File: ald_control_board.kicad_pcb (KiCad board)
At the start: 2 copper layers, 70 parts, among them J1 PWR_24V_IN, J10 MFC_DB15, J11 VACUUM_GAUGE_8PIN, J2 PWR_12V_IN, J3 PWR_5V_IN, J4 PWR_±15V_IN, J5 J_FORELINE_VALVE, J6 J_PRECURSOR_A, J7 J_N2_PURGE, J8 J_SPARE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

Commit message: im so happy
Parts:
- removed TP2: TestPoint, TestPoint:TestPoint_Loop_D2.50mm_Drill1.0mm
- moved TP3 101.0 mm to (228.4, 125.0)
- moved TP7 97.0 mm to (224.7, 137.0)
- moved C12 94.8 mm to (212.2, 135.4), turned to 180 degrees
- moved R3 94.6 mm to (216.5, 125.2)
- moved R6 93.6 mm to (216.5, 135.4)
- moved TP5 89.6 mm to (216.8, 130.2)
- moved J9 87.5 mm to (220.7, 122.6)
- moved R7 82.0 mm to (225.3, 141.1), turned to 180 degrees
- moved R2 81.9 mm to (224.7, 122.4)
- moved C13 81.3 mm to (230.0, 141.1)
- moved TP1 78.2 mm to (216.5, 122.2)
- moved TP8 76.7 mm to (215.4, 139.7)
- moved R4 76.5 mm to (224.7, 127.8), turned to 180 degrees
- moved R5 75.3 mm to (224.7, 132.9), turned to 180 degrees
- moved C11 75.2 mm to (229.6, 132.9)
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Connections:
- C1 pad 1: GND_PWR -> +24V
- C10 pad 2: /power_input/-15V -> -15V
- C12 pad 1: /daq_interface/AI_PRESSURE_FILT -> /vacuum_gauge_interface/AI_PRESSURE_FILT
- C2 pad 2: GND_PWR -> +24V
- C20 pad 1: /vacuum_gauge_interface/+24V -> +24V
- C21 pad 1: /vacuum_gauge_interface/+24V -> +24V
- C3 pad 2: GND_PWR -> +12V
- C4 pad 1: GND_PWR -> +12V
- C5 pad 1: GND_SIG -> +5V
- C6 pad 1: GND_SIG -> +5V
- C7 pad 1: /power_input/+15V -> +15V
- C8 pad 1: /power_input/+15V -> +15V
- C9 pad 1: /power_input/-15V -> -15V
- F1 pad 2: /power_input/+24V_IN -> +24V
- F2 pad 2: /power_input/+12V_IN -> +12V
- J1 pad 1: /power_input/+24V_IN -> +24V
- J11 pad 1: /vacuum_gauge_interface/+24V -> +24V
- J2 pad 1: /power_input/+12V_IN -> +12V
- J3 pad 1: GND_SIG -> +5V
- J4 pad 1: /power_input/+15V -> +15V
- J4 pad 3: /power_input/-15V -> -15V
- J5 pad 2: GNDPWR -> GND_PWR
- J9 pad 6: /daq_interface/AI_PRESSURE -> /vacuum_gauge_interface/AI_PRESSURE
- K1 pad 1: (no net) -> Net-(J6-Pin_1)
- K1 pad 2: (no net) -> /relay_board/P0.1
- K1 pad 3: (no net) -> GND_PWR
- K1 pad 5: (no net) -> +24V
- K2 pad 1: (no net) -> Net-(J5-Pin_1)
- K2 pad 2: (no net) -> /relay_board/P0.0
- K2 pad 3: (no net) -> GND_PWR
- K2 pad 5: (no net) -> +12V
- K3 pad 1: (no net) -> Net-(J7-Pin_1)
- K3 pad 3: (no net) -> GND_PWR
- K3 pad 5: (no net) -> +24V
- K4 pad 1: (no net) -> Net-(J8-Pin_1)
- K4 pad 2: (no net) -> /relay_board/P0.3
- K4 pad 3: (no net) -> GND_PWR
- K4 pad 5: (no net) -> +24V
- R6 pad 1: /daq_interface/AI_PRESSURE_FILT -> /vacuum_gauge_interface/AI_PRESSURE_FILT
- R6 pad 2: /daq_interface/AI_PRESSURE -> /vacuum_gauge_interface/AI_PRESSURE
- R8 pad 1: AO_MFC_SETPOINT -> /daq_interface/AO_MFC_SETPOINT
- R9 pad 1: AI_MFC_FLOW -> /daq_interface/AI_MFC_FLOW
- TP15 pad 1: /vacuum_gauge_interface/+24V -> +24V
- TP7 pad 1: /daq_interface/AI_PRESSURE -> /vacuum_gauge_interface/AI_PRESSURE
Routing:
- net +24V: track 0.00 -> 302.2 mm
- net +15V: track 0.00 -> 287.1 mm
- net -15V: track 0.00 -> 267.0 mm
- net +12V: track 0.00 -> 113.0 mm
- net /daq_interface/AI_MFC_FLOW: track 0.00 -> 102.9 mm
- net /daq_interface/AO_MFC_SETPOINT: track 0.00 -> 90.1 mm
- net GND_PWR: track 0.00 -> 88.3 mm, vias 0 -> 2
- net Net-(J8-Pin_1): track 0.00 -> 28.0 mm
- net Net-(J6-Pin_1): track 0.00 -> 27.5 mm
- net Net-(J7-Pin_1): track 0.00 -> 27.3 mm
- net Net-(J5-Pin_1): track 0.00 -> 26.7 mm
- net GND_SIG: track 0.00 -> 19.1 mm
- net +5V: track 0.00 -> 16.4 mm
- net Net-(C15-Pad1): track 0.00 -> 16.3 mm
- net CHASSIS_GND: track 0.00 -> 15.5 mm, vias 0 -> 1
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- added copper zone on B.Cu, net CHASSIS_GND
- added copper zone on B.Cu, net GND_PWR
- added copper zone on B.Cu, net GND_SIG
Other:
- board outline added: 204.9 x 111.1 mm

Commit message: Hopefully finalized PCB design and other files
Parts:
- added REF**: MountingHole_3.2mm_M3_Pad_Via, MountingHole:MountingHole_3.2mm_M3_Pad_Via, F.Cu at (61.5, 47.5)
- added REF**: MountingHole_3.2mm_M3_Pad_Via, MountingHole:MountingHole_3.2mm_M3_Pad_Via, F.Cu at (252.0, 47.0)
- added REF**: MountingHole_3.2mm_M3_Pad_Via, MountingHole:MountingHole_3.2mm_M3_Pad_Via, F.Cu at (62.0, 145.0)
- added REF**: MountingHole_3.2mm_M3_Pad_Via, MountingHole:MountingHole_3.2mm_M3_Pad_Via, F.Cu at (252.5, 145.0)
- moved TP13 33.7 mm to (221.0, 78.0)
- moved C7 15.9 mm to (76.5, 117.0)
- moved C9 15.9 mm to (84.0, 117.5)
- moved C10 15.9 mm to (84.9, 124.5)
- moved C8 15.9 mm to (75.5, 125.5)
- moved J3 7.27 mm to (66.0, 100.0), turned to -90 degrees
- moved J2 5.50 mm to (66.0, 86.5), turned to -90 degrees
- moved C5 5.28 mm to (82.4, 103.0)
- moved C6 5.28 mm to (75.0, 103.0)
- moved J1 5.17 mm to (65.3, 63.0), turned to -90 degrees
- moved J5 4.81 mm to (161.5, 61.5), turned to 180 degrees
- moved J7 4.54 mm to (160.0, 106.1), turned to 90 degrees
- moved J4 4.15 mm to (66.5, 116.4), turned to -90 degrees
- moved C2 3.65 mm to (66.0, 56.0)
- moved J6 2.79 mm to (159.5, 84.1), turned to 90 degrees
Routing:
- net GND_SIG: track 19.1 -> 410.5 mm, vias 0 -> 11
- net GND_PWR: track 88.3 -> 279.4 mm, vias 2 -> 4
- net /vacuum_gauge_interface/AI_PRESSURE_FILT: track 5.55 -> 118.2 mm, vias 0 -> 2
- net /vacuum_gauge_interface/AI_PRESSURE: track 13.7 -> 106.0 mm, vias 0 -> 2
- net +15V: track 287.1 -> 238.6 mm, vias 0 -> 2
- net -15V: track 267.0 -> 222.4 mm, vias 0 -> 4
- net +24V: track 302.2 -> 293.0 mm
- net +12V: track 113.0 -> 106.7 mm
- net Net-(J5-Pin_1): track 26.7 -> 32.9 mm
- net Net-(J6-Pin_1): track 27.5 -> 33.1 mm
- net Net-(C18-Pad1): track 0.00 -> 5.44 mm
- net Net-(C16-Pad2): track 0.00 -> 4.68 mm
- net Net-(C14-Pad1): track 13.5 -> 16.9 mm
- net Net-(C15-Pad1): track 16.3 -> 18.7 mm
- net +5V: track 16.4 -> 18.1 mm
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
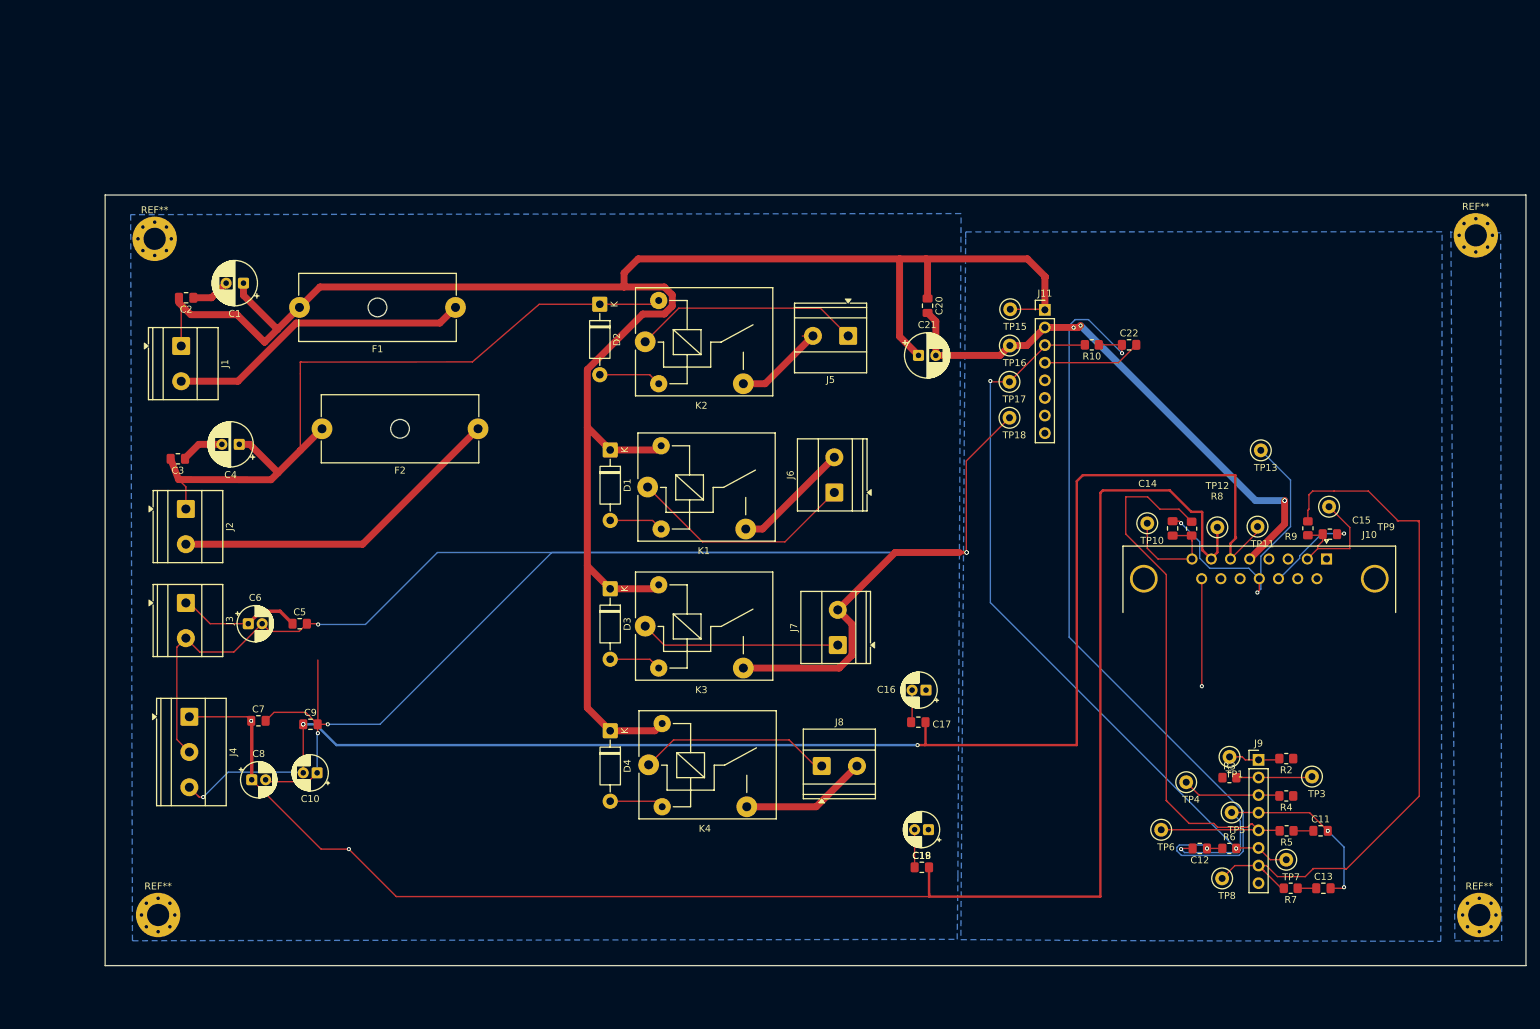
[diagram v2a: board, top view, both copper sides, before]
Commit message: rotated MFC and 10 pin daq
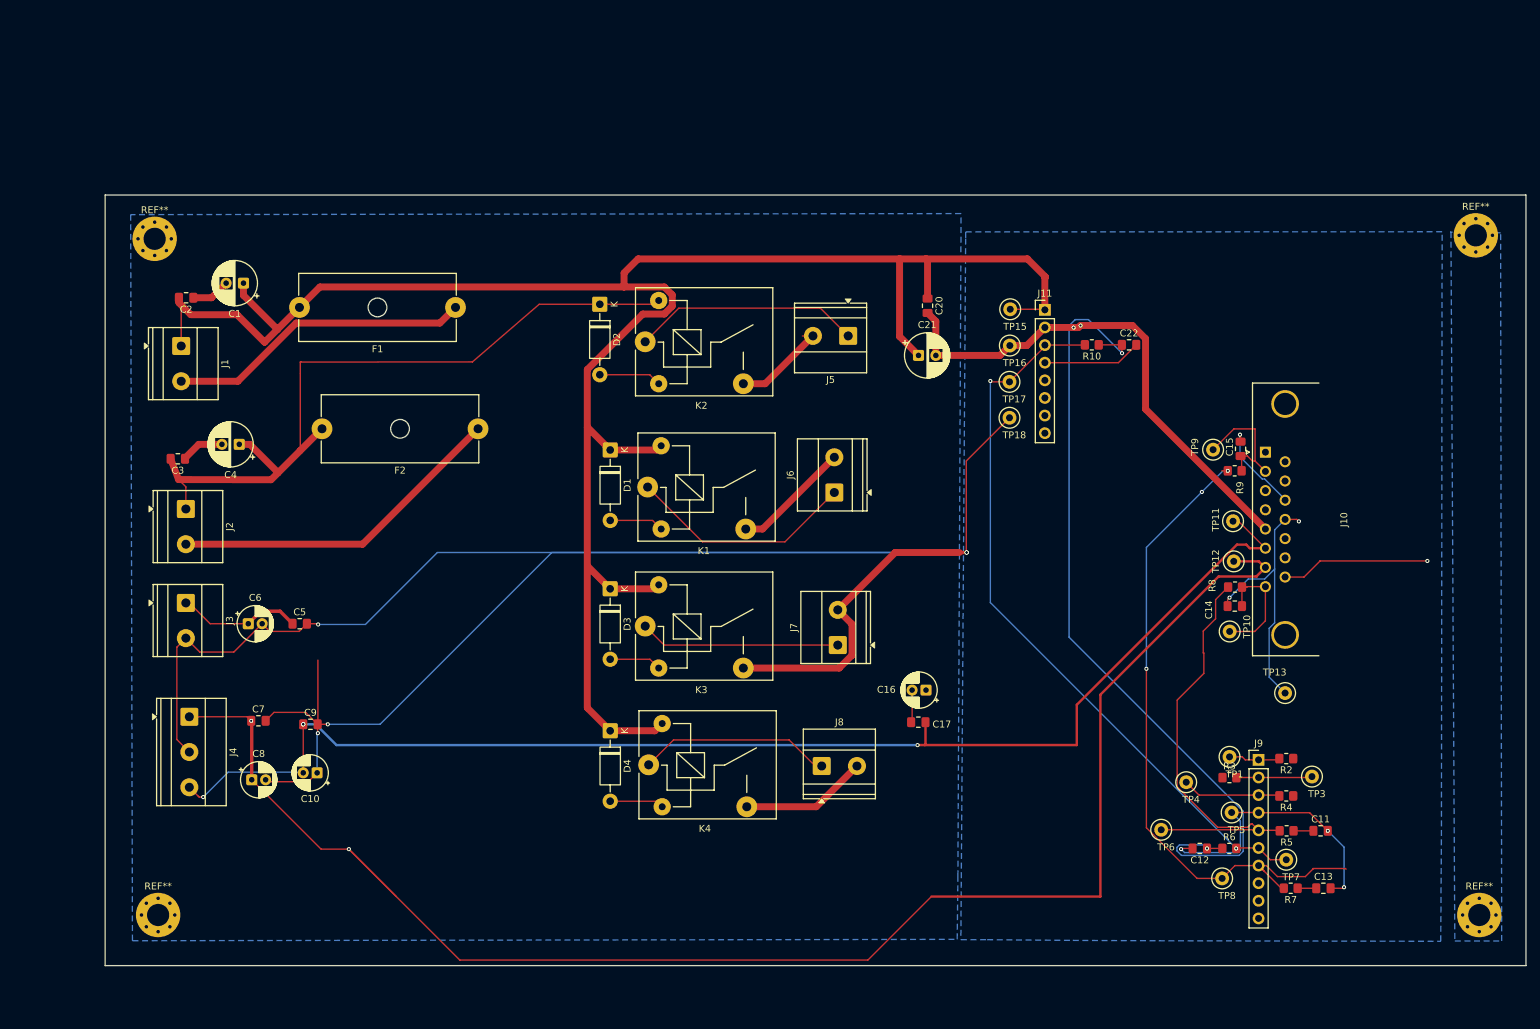
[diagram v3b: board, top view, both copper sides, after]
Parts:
- removed C18: 0.1µF, Capacitor_SMD:C_0805_2012Metric_Pad1.18x1.45mm_HandSolder
- removed C19: 10µF, Capacitor_THT:CP_Radial_D5.0mm_P2.00mm
- J9: footprint Connector_PinHeader_2.54mm:PinHeader_1x08_P2.54mm_Vertical -> Connector_PinHeader_2.54mm:PinHeader_1x10_P2.54mm_Vertical
- moved TP13 35.2 mm to (224.5, 113.0), turned to 90 degrees
- moved TP10 19.6 mm to (216.5, 104.1), turned to 90 degrees
- moved TP9 18.6 mm to (214.1, 77.9), turned to 90 degrees
- moved C15 17.8 mm to (218.1, 77.8), turned to 90 degrees
- moved J10 17.7 mm to (221.7, 78.3), turned to 90 degrees
- moved C14 14.4 mm to (217.2, 100.5), turned to 180 degrees
- moved R9 13.4 mm to (217.2, 81.0), turned to 0 degrees
- moved R8 10.5 mm to (217.3, 97.7), turned to 0 degrees
- moved TP12 5.44 mm to (217.1, 94.0), turned to 90 degrees
- moved TP11 3.62 mm to (217.0, 88.2), turned to 90 degrees
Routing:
- net -15V: track 222.4 -> 191.5 mm
- net /daq_interface/AO_MFC_SETPOINT: track 90.1 -> 63.9 mm
- net +15V: track 238.6 -> 230.5 mm
- net CHASSIS_GND: track 15.5 -> 21.5 mm
- net GND_PWR: track 279.4 -> 273.7 mm, vias 4 -> 2
- net Net-(C18-Pad1): track 5.44 -> 0.00 mm
- net /daq_interface/AI_MFC_FLOW: track 102.9 -> 97.6 mm, vias 0 -> 3
- net GND_SIG: track 410.5 -> 405.4 mm

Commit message: hopefully finalized pcb
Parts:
- added C18: 10µF, Capacitor_THT:CP_Radial_D5.0mm_P2.00mm, F.Cu at (176.0, 134.0)
- added C19: 0.1µF, Capacitor_SMD:C_0805_2012Metric_Pad1.18x1.45mm_HandSolder, F.Cu at (174.9, 138.6)
- added D4: Diode, Diode_THT:D_DO-41_SOD81_P10.16mm_Horizontal, F.Cu at (126.5, 136.9)
- added J12: J_RELAY, TerminalBlock_Phoenix:TerminalBlock_Phoenix_MKDS-1,5-2-5.08_1x02_P5.08mm_Horizontal, F.Cu at (156.9, 142.1)
- added K5: Relay 5, Relay_THT:Relay_SPST_SANYOU_SRD_Series_Form_A, F.Cu at (131.9, 141.9)
- moved J8 4.47 mm to (161.7, 125.5), turned to 90 degrees
- moved C16 1.36 mm to (174.0, 112.0)
- moved C17 1.36 mm to (172.8, 116.6)
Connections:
- J9 pad 9: (no net) -> DO_RELAY
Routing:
- net GND_PWR: track 273.7 -> 303.0 mm
- net Net-(J12-Pin_1): track 0.00 -> 28.0 mm
- net +24V: track 293.0 -> 320.6 mm
- net PO.4: track 0.00 -> 7.83 mm
- net Net-(J8-Pin_1): track 28.0 -> 32.8 mm
- net +15V: track 230.5 -> 235.2 mm
- net Net-(C18-Pad1): track 0.00 -> 4.68 mm
- net -15V: track 191.5 -> 192.8 mm
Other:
- board size 204.9 x 111.1 mm -> 204.9 x 114.6 mm
- board text added: "D5"
- board text added: "K"

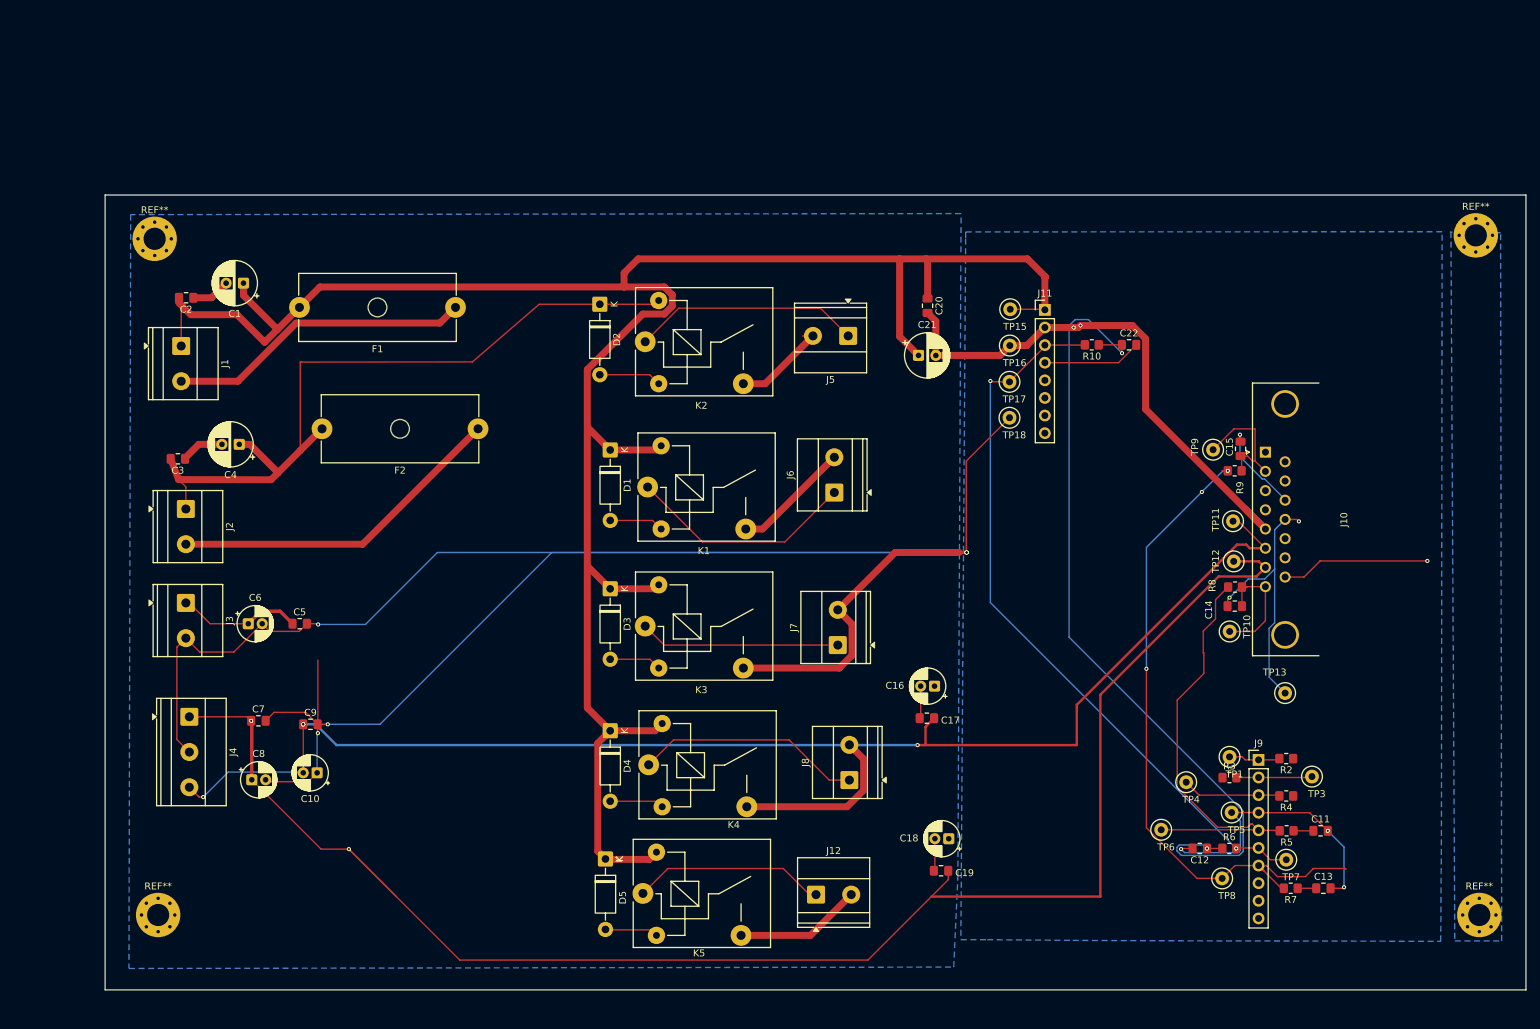
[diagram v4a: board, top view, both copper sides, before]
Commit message: added cat 5 and fixed some b.cu traces for -15v
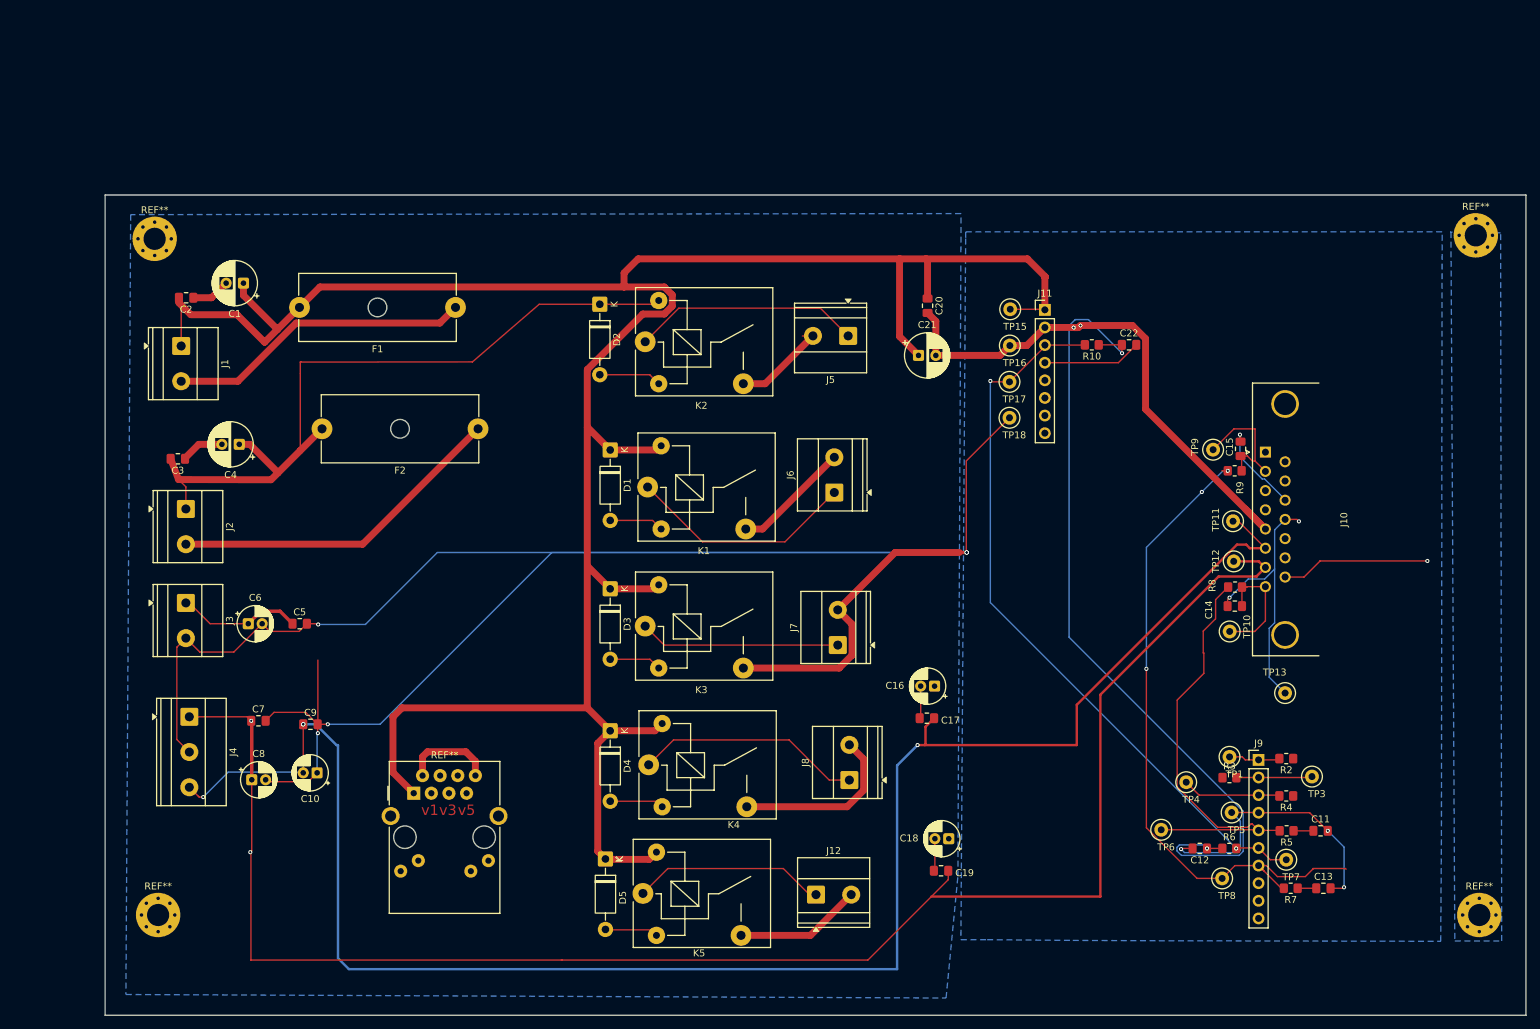
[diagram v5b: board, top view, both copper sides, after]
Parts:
- added REF**: RJ45_Amphenol_RJMG1BD3B8K1ANR, Connector_RJ:RJ45_Amphenol_RJMG1BD3B8K1ANR, F.Cu at (98.9, 127.4)
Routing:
- net -15V: track 192.8 -> 254.7 mm
- net +24V: track 320.6 -> 361.4 mm
- net GND_PWR: track 303.0 -> 316.3 mm
- net +15V: track 235.2 -> 241.2 mm
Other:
- board size 204.9 x 114.6 mm -> 204.9 x 118.3 mm
- board text added: "v1"
- board text added: "v3"
- board text added: "v5"
